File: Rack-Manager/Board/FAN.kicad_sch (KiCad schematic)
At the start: 8 parts, among them J3 Conn_01x03_Pin, M1 Fan_4pin, U10 DMG6601

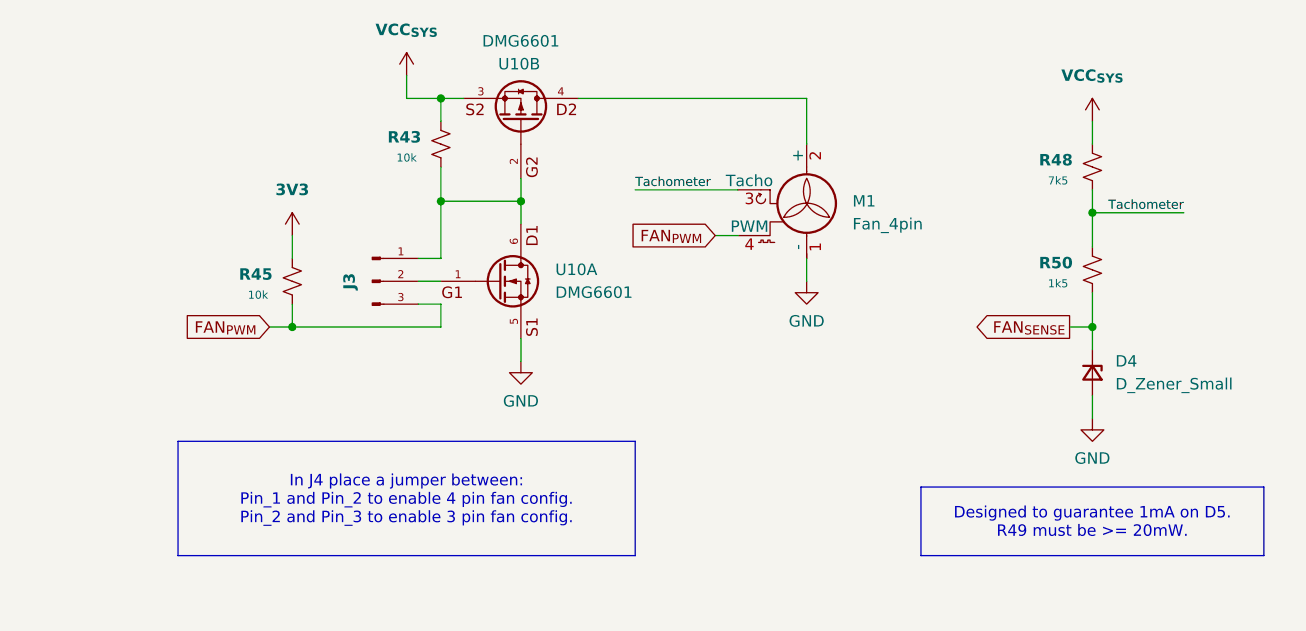
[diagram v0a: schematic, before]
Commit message: Created dedicated FAN file
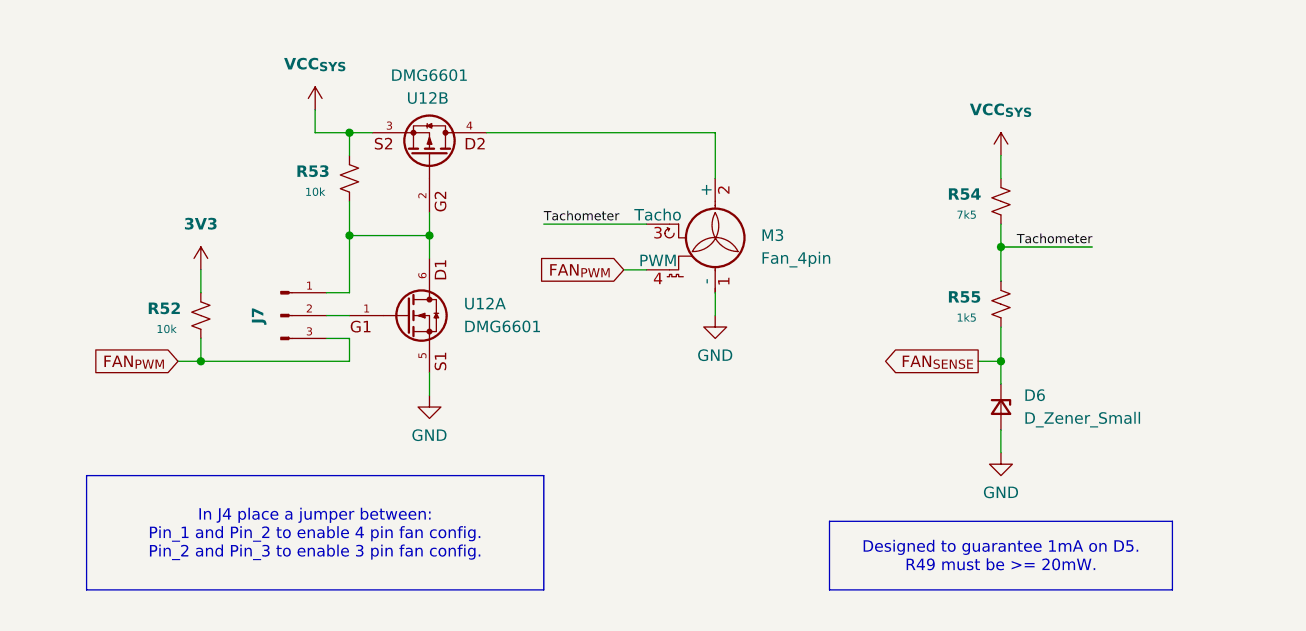
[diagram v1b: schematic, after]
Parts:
- removed D4: D_Zener_Small, Diode_SMD:D_SOD-123, symbol Device:D_Zener_Small
- removed J3: Conn_01x03_Pin, Connector_PinSocket_2.54mm:PinSocket_1x03_P2.54mm_Vertical, symbol Connector:Conn_01x03_Pin
- removed M1: Fan_4pin, Connector:FanPinHeader_1x04_P2.54mm_Vertical, symbol Motor:Fan_4pin
- removed R43, R45: 10k, Resistor_SMD:R_0402_1005Metric, symbol Device:R_Small_US
- removed R48: 7k5, Resistor_SMD:R_0402_1005Metric, symbol Device:R_Small_US
- removed R50: 1k5, Resistor_SMD:R_0402_1005Metric, symbol Device:R_Small_US
- removed U10: DMG6601, symbol Diodes:DMG6601
- added D6: D_Zener_Small, Diode_SMD:D_SOD-123, symbol Device:D_Zener_Small
- added J7: Conn_01x03_Pin, Connector_PinSocket_2.54mm:PinSocket_1x03_P2.54mm_Vertical, symbol Connector:Conn_01x03_Pin
- added M3: Fan_4pin, Connector:FanPinHeader_1x04_P2.54mm_Vertical, symbol Motor:Fan_4pin
- added R52, R53: 10k, Resistor_SMD:R_0402_1005Metric, symbol Device:R_Small_US
- added R54: 7k5, Resistor_SMD:R_0402_1005Metric, symbol Device:R_Small_US
- added R55: 1k5, Resistor_SMD:R_0402_1005Metric, symbol Device:R_Small_US
- added U12: DMG6601, symbol Diodes:DMG6601
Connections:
- net 3V3: now also R52.2
- net FAN_{PWM}: now also J7.3 (Pin_3), M3.4 (PWM), R52.1
- net FAN_{SENSE}: now also D6.1 (K), R55.1
- net GND: now also D6.2 (A), M3.1 (-), U12.5
- net Tachometer: now also M3.3 (Tacho), R54.1, R55.2
- net VCC_{SYS}: now also R53.2, R54.2, U12.3
- new net: J7.1 (Pin_1), R53.1, U12.2, U12.6
- new net: M3.2 (+), U12.4
- new net: J7.2 (Pin_2), U12.1
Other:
- title: Bus Power + Signal Output and Connectors -> (none)

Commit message: Fixed FAN control link mixed with bus output file
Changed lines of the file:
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@@
 	(generator_version "9.0")
 	(paper "A4")
-	(text_box "Designed to guarantee 1mA on D5.\nR49 must be >= 20mW."
+	(text_box "Designed to guarantee 1mA on D5.\nR54 must be >= 20mW."
 		(exclude_from_sim no)
 		(at 161.29 123.19 0)

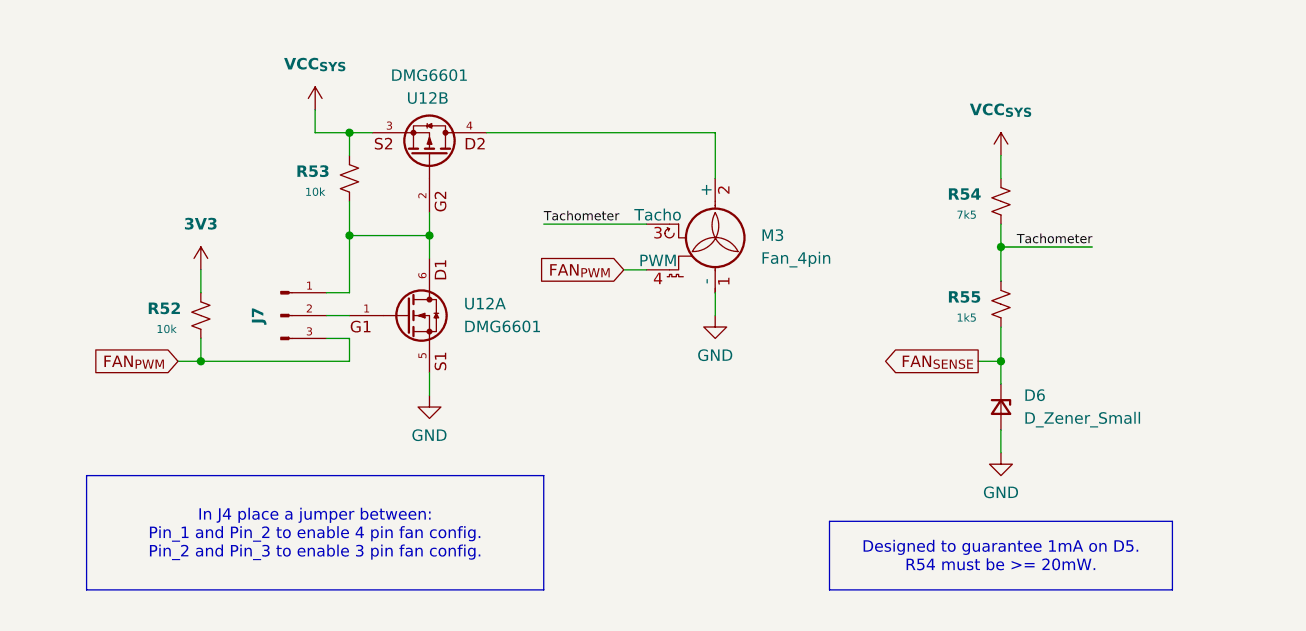
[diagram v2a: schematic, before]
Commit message: Added RS485 protection data as task describe and fixed stuff around
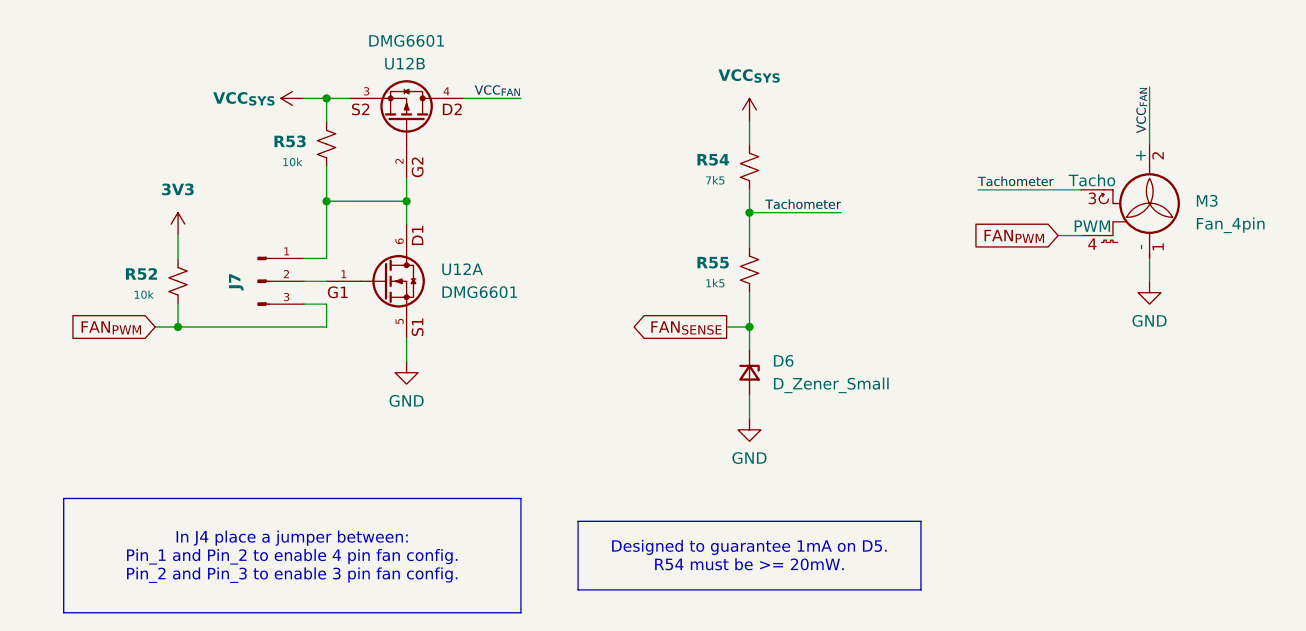
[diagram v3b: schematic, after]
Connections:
- net VCC_{FAN}: now reaches M3.2 (+), U12.4
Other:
- moved on the sheet: D6, J7, M3, R52, R53, R54, R55, U12A, U12B

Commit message: Fixed volteage divider for fan tachometer and fixed other pull-x and divider for the microcontroller
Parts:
- removed D6: D_Zener_Small, Diode_SMD:D_SOD-123, symbol Device:D_Zener_Small
- removed R54: 7k5, Resistor_SMD:R_0402_1005Metric, symbol Device:R_Small_US
- removed R55: 1k5, Resistor_SMD:R_0402_1005Metric, symbol Device:R_Small_US
- added D4: PMEG3030, Diode_SMD:D_SOD-128, symbol Device:D_Schottky_Small
- added R69: 10k, Resistor_SMD:R_0402_1005Metric, symbol Device:R_Small_US
- added R73: 1k, Resistor_SMD:R_0402_1005Metric, symbol Device:R_Small_US
- R53: value 10k -> 100k
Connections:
- net 3V3: now also R69.1
- net FAN_{SENSE}: now also R73.1
- net VCC_{FAN}: now also D4.1 (K); no longer U12.4
- net Tachometer: no longer names the net of M3.3 (Tacho)
- net Tachometer: now also R69.2, R73.2
- new net: D4.2 (A), U12.4
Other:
- moved on the sheet: M3
